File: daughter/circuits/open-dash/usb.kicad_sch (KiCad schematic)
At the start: 15 parts, among them J15 USB_MINI_B, J16 Conn_02x02_Counter_Clockwise, Q1 Crystal_12Mhz, Q2 Q_SS8050, Q39 Q_SS8550, U12 CH340T(SSOP20W)

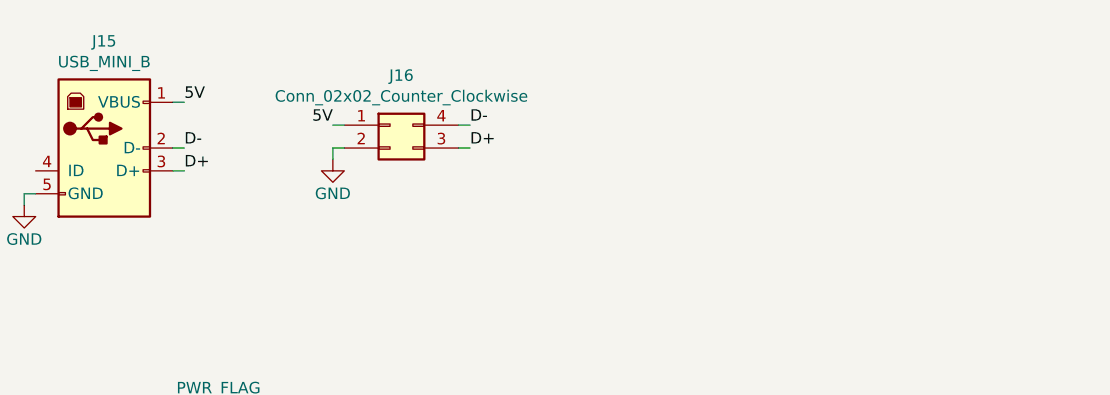
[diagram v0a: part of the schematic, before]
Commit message: Updated hvac circuit
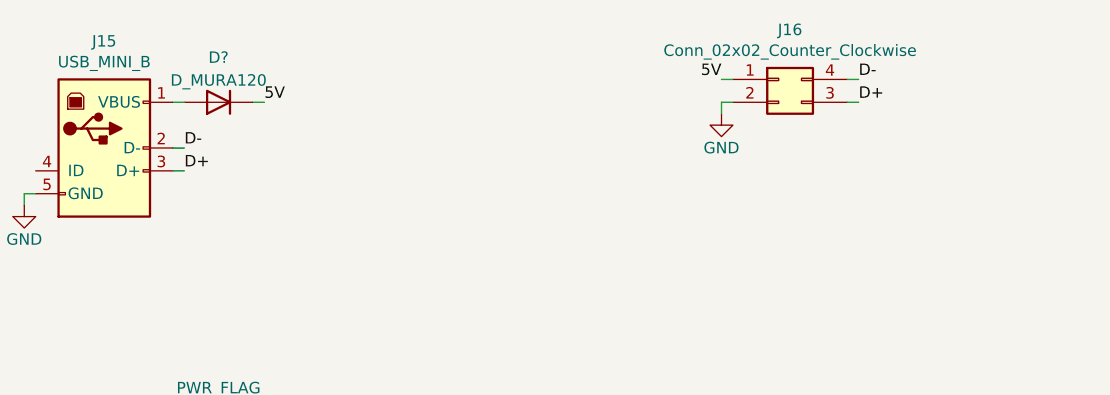
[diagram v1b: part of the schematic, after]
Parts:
- added D?: D_MURA120, Diode_SMD:D_SMA_Handsoldering, symbol Open Automation:D_MURA120
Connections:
- net 5V: now also D?.1 (K); no longer J15.1 (VBUS)
- new net: D?.2 (A), J15.1 (VBUS)
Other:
- moved on the sheet: J16
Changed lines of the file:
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@@
   (no_connect (at 135.89 86.36))
   (no_connect (at 135.89 99.06))
-  (wire (pts (xy 85.09 29.21) (xy 86.36 29.21))
+  (wire (pts (xy 128.27 24.13) (xy 129.54 24.13))
     (stroke (width 0) (type default) (color 0 0 0 0))
   )
@@
     (stroke (width 0) (type default) (color 0 0 0 0))
   )
-  (wire (pts (xy 85.09 26.67) (xy 86.36 26.67))
+  (wire (pts (xy 128.27 21.59) (xy 129.54 21.59))
     (stroke (width 0) (type default) (color 0 0 0 0))
   )
@@
     (stroke (width 0) (type default) (color 0 0 0 0))
   )
-  (wire (pts (xy 85.09 30.48) (xy 85.09 29.21))
+  (wire (pts (xy 128.27 25.4) (xy 128.27 24.13))
     (stroke (width 0) (type default) (color 0 0 0 0))
   )
@@
     (stroke (width 0) (type default) (color 0 0 0 0))
   )
-  (wire (pts (xy 100.33 29.21) (xy 99.06 29.21))
+  (wire (pts (xy 143.51 24.13) (xy 142.24 24.13))
     (stroke (width 0) (type default) (color 0 0 0 0))
   )
@@
     (stroke (width 0) (type default) (color 0 0 0 0))
   )
-  (wire (pts (xy 100.33 26.67) (xy 99.06 26.67))
+  (wire (pts (xy 143.51 21.59) (xy 142.24 21.59))
     (stroke (width 0) (type default) (color 0 0 0 0))
   )
@@
   )
   (wire (pts (xy 130.81 68.58) (xy 184.15 68.58))
+    (stroke (width 0) (type default) (color 0 0 0 0))
+  )
+  (wire (pts (xy 76.2 24.13) (xy 77.47 24.13))
     (stroke (width 0) (type default) (color 0 0 0 0))
   )
@@
     (effects (font (size 1.27 1.27)) (justify left bottom))
   )
-  (label "5V" (at 85.09 26.67 180)
+  (label "5V" (at 128.27 21.59 180)
     (effects (font (size 1.27 1.27)) (justify right bottom))
   )
@@
     (effects (font (size 1.27 1.27) (thickness 0.254) bold) (justify left bottom))
   )
-  (label "D+" (at 100.33 29.21 0)
+  (label "D+" (at 143.51 24.13 0)
     (effects (font (size 1.27 1.27)) (justify left bottom))
   )
@@
     (effects (font (size 1.27 1.27)) (justify left bottom))
   )
-  (label "5V" (at 68.58 24.13 0)
+  (label "5V" (at 77.47 24.13 0)
     (effects (font (size 1.27 1.27)) (justify left bottom))
   )
@@
     (effects (font (size 1.27 1.27)) (justify left bottom))
   )
-  (label "D-" (at 100.33 26.67 0)
+  (label "D-" (at 143.51 21.59 0)
     (effects (font (size 1.27 1.27)) (justify left bottom))
   )
@@
     (pin "5")
   )
-  (symbol (lib_id "power:GND") (at 72.39 106.68 0)
+  (symbol (lib_id "power:GND") (at 72.39 106.68 0) (unit 1)
     (in_bom yes) (on_board yes)
     (property "Reference" "#PWR0113" (id 0) (at 72.39 113.03 0)
@@
     (pin "1")
   )
-  (symbol (lib_id "power:GND") (at 50.8 35.56 0)
+  (symbol (lib_id "power:GND") (at 50.8 35.56 0) (unit 1)
     (in_bom yes) (on_board yes)
     (property "Reference" "#PWR0116" (id 0) (at 50.8 41.91 0)
@@
     (pin "1")
   )
-  (symbol (lib_id "power:GND") (at 80.01 76.2 270)
+  (symbol (lib_id "power:GND") (at 80.01 76.2 270) (unit 1)
     (in_bom yes) (on_board yes)
     (property "Reference" "#PWR0119" (id 0) (at 73.66 76.2 0)
@@
     (pin "1")
   )
-  (symbol (lib_id "power:GND") (at 80.01 78.74 270)
+  (symbol (lib_id "power:GND") (at 80.01 78.74 270) (unit 1)
     (in_bom yes) (on_board yes)
     (property "Reference" "#PWR0127" (id 0) (at 73.66 78.74 0)
@@
     (pin "1")
   )
-  (symbol (lib_id "power:GND") (at 80.01 83.82 270)
+  (symbol (lib_id "power:GND") (at 80.01 83.82 270) (unit 1)
     (in_bom yes) (on_board yes)
     (property "Reference" "#PWR0150" (id 0) (at 73.66 83.82 0)
@@
     (pin "9")
   )
-  (symbol (lib_id "open-dash-daughterboard-rescue:Conn_02x02_Counter_Clockwise-Connector_Generic") (at 91.44 26.67 0)
-    (in_bom yes) (on_board yes)
-    (property "Reference" "J16" (id 0) (at 92.71 21.1582 0))
-    (property "Value" "Conn_02x02_Counter_Clockwise" (id 1) (at 92.71 23.4696 0))
-    (property "Footprint" "Connector_PinHeader_2.54mm:PinHeader_2x02_P2.54mm_Vertical" (id 2) (at 91.44 26.67 0)
-      (effects (font (size 1.27 1.27)) hide)
-    )
-    (property "Datasheet" "~" (id 3) (at 91.44 26.67 0)
+  (symbol (lib_id "open-dash-daughterboard-rescue:Conn_02x02_Counter_Clockwise-Connector_Generic") (at 134.62 21.59 0) (unit 1)
+    (in_bom yes) (on_board yes)
+    (property "Reference" "J16" (id 0) (at 135.89 16.0782 0))
+    (property "Value" "Conn_02x02_Counter_Clockwise" (id 1) (at 135.89 18.3896 0))
+    (property "Footprint" "Connector_PinHeader_2.54mm:PinHeader_2x02_P2.54mm_Vertical" (id 2) (at 134.62 21.59 0)
+      (effects (font (size 1.27 1.27)) hide)
+    )
+    (property "Datasheet" "~" (id 3) (at 134.62 21.59 0)
       (effects (font (size 1.27 1.27)) hide)
     )
@@
     (pin "4")
   )
-  (symbol (lib_id "power:GND") (at 85.09 30.48 0)
-    (in_bom yes) (on_board yes)
-    (property "Reference" "#PWR0110" (id 0) (at 85.09 36.83 0)
-      (effects (font (size 1.27 1.27)) hide)
-    )
-    (property "Value" "GND" (id 1) (at 85.09 34.29 0))
-    (property "Footprint" "" (id 2) (at 85.09 30.48 0)
-      (effects (font (size 1.27 1.27)) hide)
-    )
-    (property "Datasheet" "" (id 3) (at 85.09 30.48 0)
-      (effects (font (size 1.27 1.27)) hide)
-    )
-    (pin "1")
+  (symbol (lib_id "power:GND") (at 128.27 25.4 0) (unit 1)
+    (in_bom yes) (on_board yes)
+    (property "Reference" "#PWR0110" (id 0) (at 128.27 31.75 0)
+      (effects (font (size 1.27 1.27)) hide)
+    )
+    (property "Value" "GND" (id 1) (at 128.27 29.21 0))
+    (property "Footprint" "" (id 2) (at 128.27 25.4 0)
+      (effects (font (size 1.27 1.27)) hide)
+    )
+    (property "Datasheet" "" (id 3) (at 128.27 25.4 0)
+      (effects (font (size 1.27 1.27)) hide)
+    )
+    (pin "1")
+  )
+  (symbol (lib_id "Open Automation:D_MURA120") (at 72.39 24.13 180) (unit 1)
+    (in_bom yes) (on_board yes) (fields_autoplaced)
+    (property "Reference" "D?" (id 0) (at 72.39 19.1602 0))
+    (property "Value" "D_MURA120" (id 1) (at 72.39 21.6971 0))
+    (property "Footprint" "Diode_SMD:D_SMA_Handsoldering" (id 2) (at 72.39 24.13 0)
+      (effects (font (size 1.27 1.27)) hide)
+    )
+    (property "Datasheet" "https://datasheet.lcsc.com/szlcsc/ON-Semicon-ON-MURA120T3G_C111832.pdf" (id 3) (at 72.39 24.13 0)
+      (effects (font (size 1.27 1.27)) hide)
+    )
+    (property "Part Number" "MURA120T3G" (id 4) (at 72.39 24.13 0)
+      (effects (font (size 1.27 1.27)) hide)
+    )
+    (property "LCSC" "C111832" (id 5) (at 72.39 24.13 0)
+      (effects (font (size 1.27 1.27)) hide)
+    )
+    (pin "1")
+    (pin "2")
   )
 )
